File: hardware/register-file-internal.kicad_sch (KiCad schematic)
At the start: 7 parts, among them U4 CD74HC670M96, U5 CD74HC670M96, U6 SN74LVC8T245DWRG4

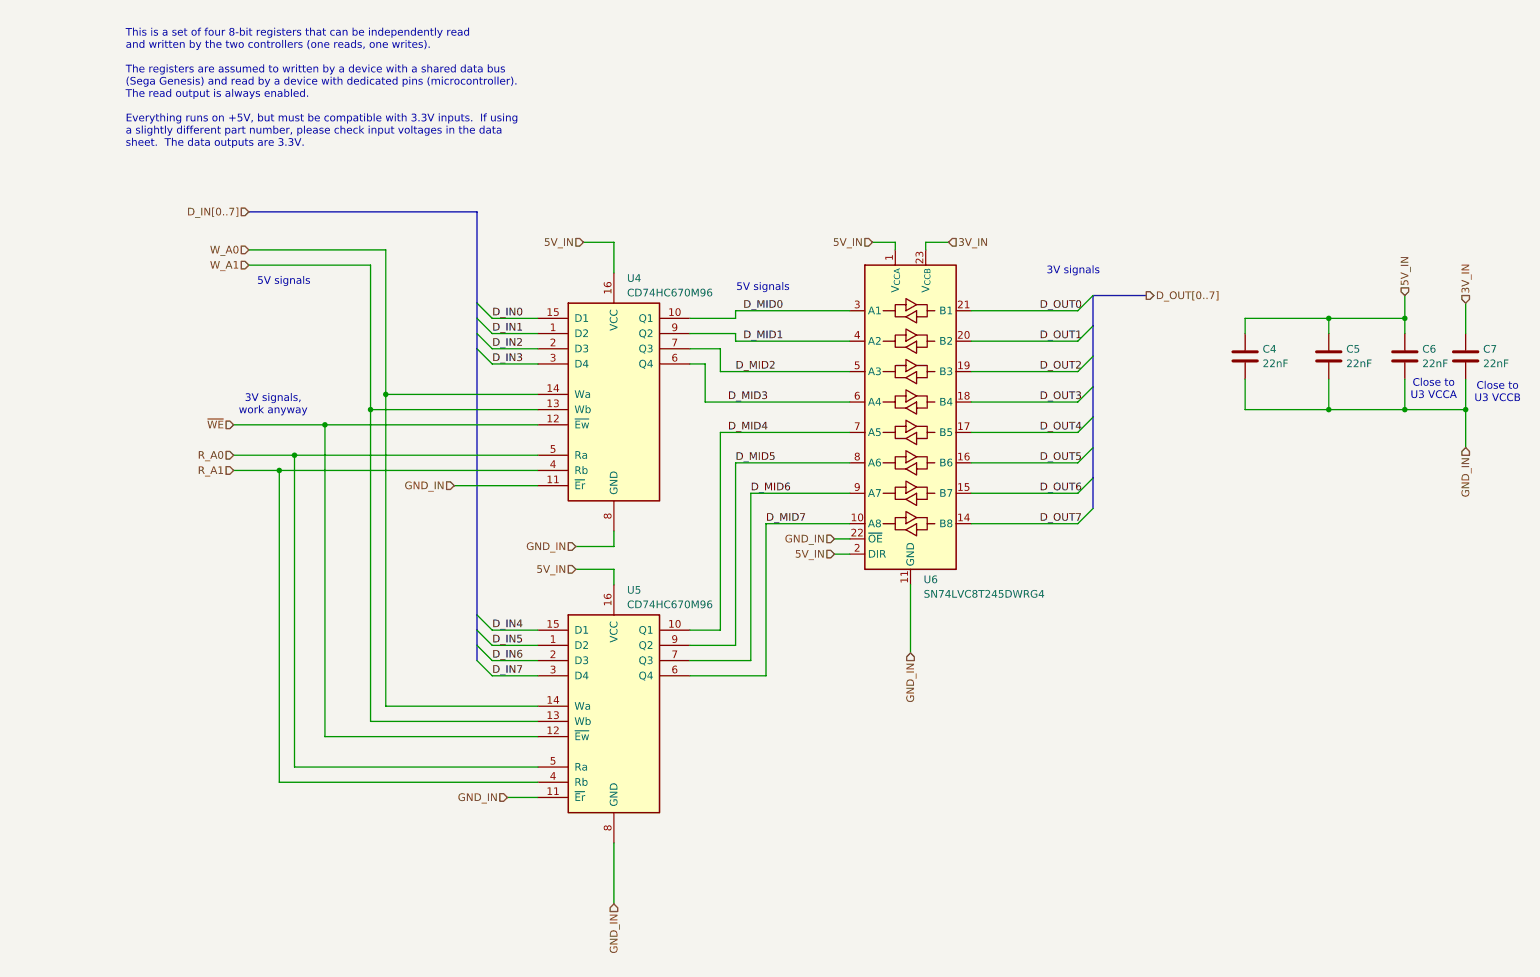
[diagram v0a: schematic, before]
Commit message: Massively reorganize board designs
Now planning to have most assembly done by JLCPCB, so trace sizes,
part selections, etc. are set accordingly.

New boards are:
 - cartridge interface & flash
 - microcontroller & registers
 - sram x2
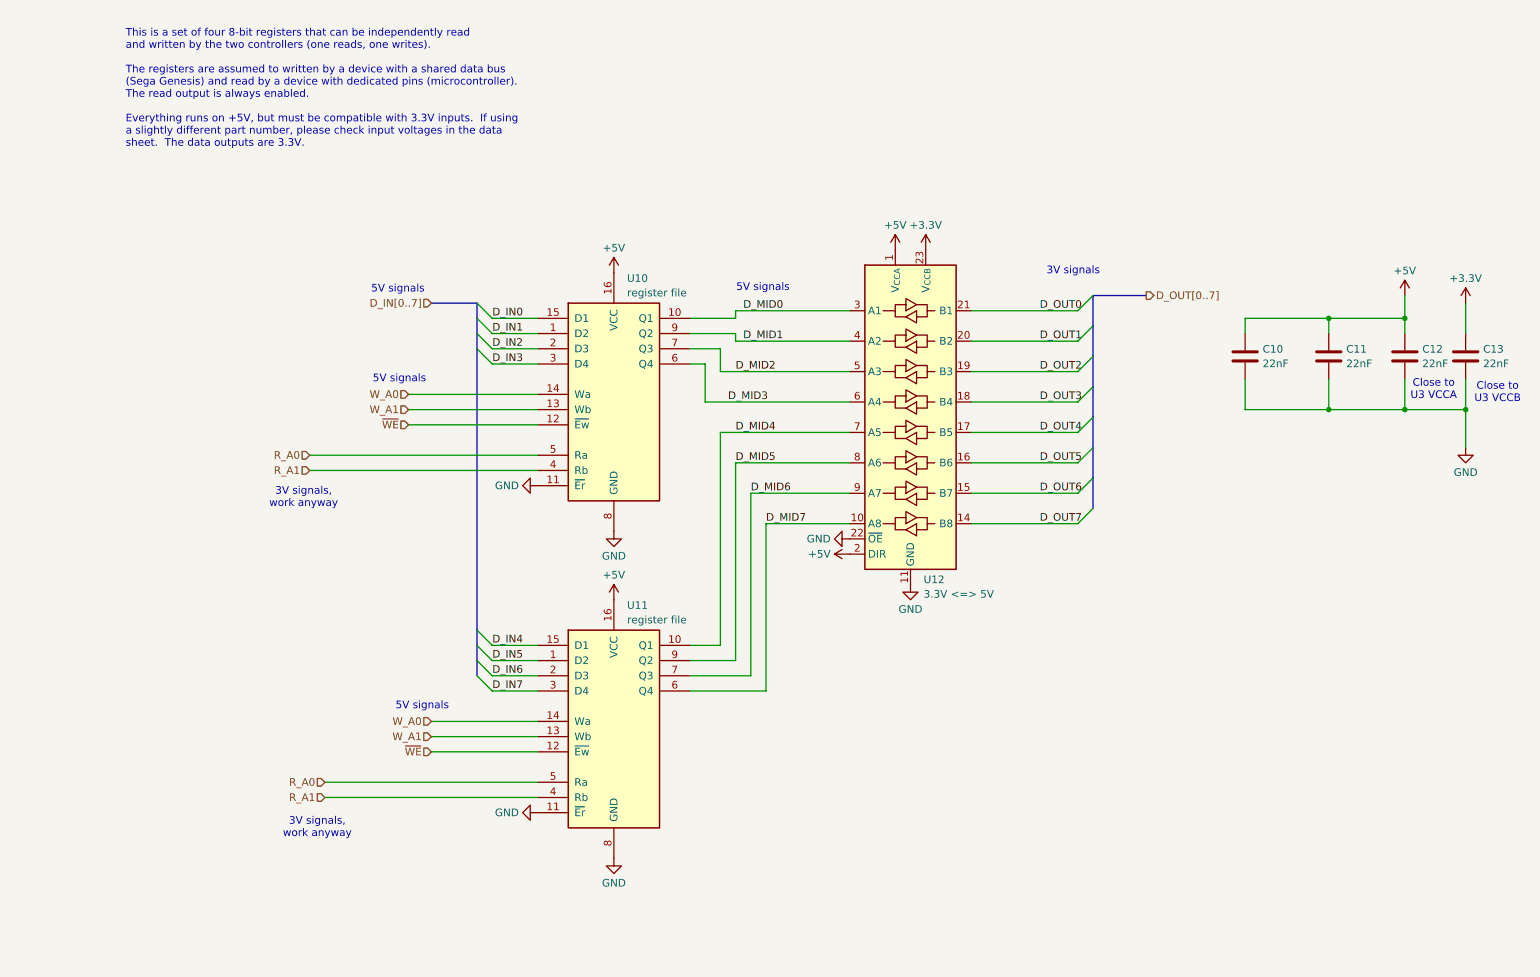
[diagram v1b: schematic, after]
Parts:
- C10: renamed from C4; JLCPCB Part Number (none) -> C21122; Mouser Part Number (none) -> 187-CL10B223KB8NNNC; Part Number (none) -> CL10B223KB8NNNC
- C11: renamed from C5; JLCPCB Part Number (none) -> C21122; Mouser Part Number (none) -> 187-CL10B223KB8NNNC; Part Number (none) -> CL10B223KB8NNNC
- C12: renamed from C6; JLCPCB Part Number (none) -> C21122; Mouser Part Number (none) -> 187-CL10B223KB8NNNC; Part Number (none) -> CL10B223KB8NNNC
- C13: renamed from C7; JLCPCB Part Number (none) -> C21122; Mouser Part Number (none) -> 187-CL10B223KB8NNNC; Part Number (none) -> CL10B223KB8NNNC
- U10: renamed from U4; value CD74HC670M96 -> register file; Mouser Part Number (none) -> 595-CD74HC670M96; Part Number (none) -> CD74HC670M96
- U11: renamed from U5; value CD74HC670M96 -> register file; Mouser Part Number (none) -> 595-CD74HC670M96; Part Number (none) -> CD74HC670M96
- U12: renamed from U6; value SN74LVC8T245DWRG4 -> 3.3V <=> 5V; footprint Package_SO:SOIC-24W_7.5x15.4mm_P1.27mm -> Package_SO:SSOP-24_5.3x8.2mm_P0.65mm; JLCPCB Part Number (none) -> C19197; Mouser Part Number (none) -> 595-SN74LVC8T245DBR; Part Number (none) -> SN74LVC8T245DBR
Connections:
- net 3V_IN renamed +3.3V
- net 5V_IN renamed +5V
- net GND_IN renamed GND
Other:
- moved on the sheet: U11

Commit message: Revise microcontroller board based on latest cart board improvements
 - Update comments
 - Segregate the Ethernet module's power supply so it can be
   disconnected if something goes wrong in a prototype
 - Update board setup to match latest cart board
 - Remove unnecessary level-shifter
 - Fix address decoder to non-latching version
 - Fix address decoder output assignment
 - Consolidate buffer ICs in register file
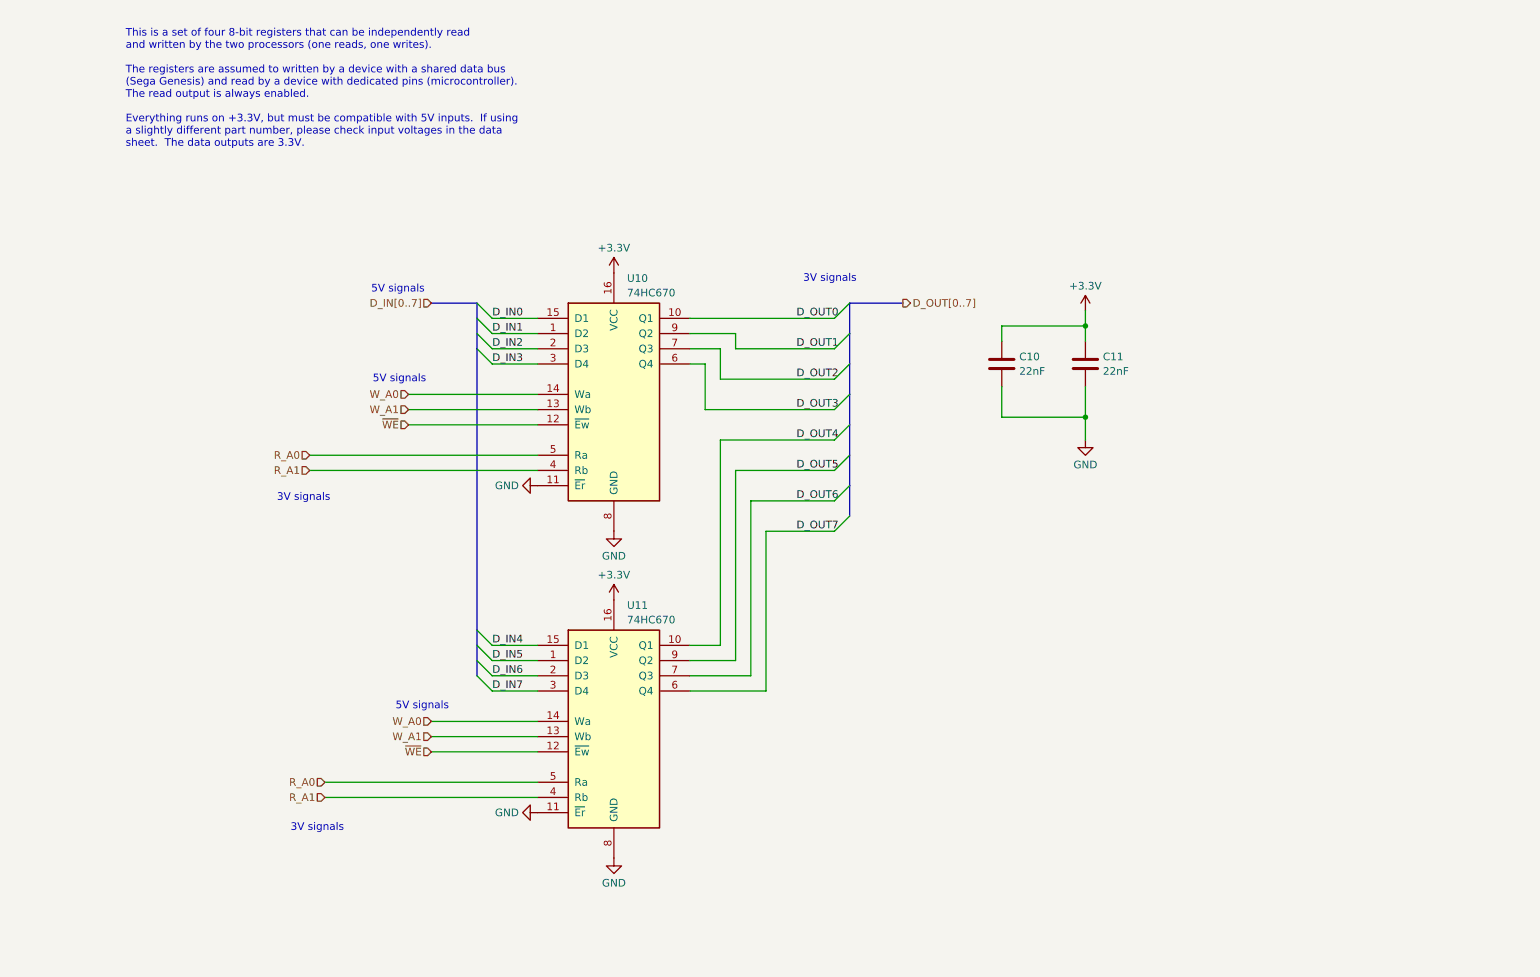
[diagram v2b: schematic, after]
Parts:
- removed C12, C13: 22nF, Capacitor_SMD:C_0603_1608Metric, symbol Device:C
- removed U12: 3.3V <=> 5V, Package_SO:SSOP-24_5.3x8.2mm_P0.65mm, symbol Logic_LevelTranslator:SN74LVC8T245
- U10, U11: value register file -> 74HC670
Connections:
- net +5V is gone; now on net +3.3V: C10.1, C11.1, U10.16 (VCC), U11.16 (VCC)
- net D_MID0 is gone; now on net D_OUT0: U10.10 (Q1)
- net D_MID1 is gone; now on net D_OUT1: U10.9 (Q2)
- net D_MID2 is gone; now on net D_OUT2: U10.7 (Q3)
- net D_MID3 is gone; now on net D_OUT3: U10.6 (Q4)
- net D_MID4 is gone; now on net D_OUT4: U11.10 (Q1)
- net D_MID5 is gone; now on net D_OUT5: U11.9 (Q2)
- net D_MID6 is gone; now on net D_OUT6: U11.7 (Q3)
- net D_MID7 is gone; now on net D_OUT7: U11.6 (Q4)
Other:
- note added: "This is a set of four 8-bit registers that can be independently read and written by the two processors (one reads, one writes). The registers are assumed to written by a device with a shared data bus (Sega Genesis) and read by a device with dedicated pins (microcontroller). The read output is always enabled. Everything runs on +3.3V, but must be compatible with 5V inputs. If using a slightly diff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"
- note removed: "3V signals, work anyway"
- note removed: "Close to U3 VCCA"
- note removed: "Close to U3 VCCB"
- note removed: "This is a set of four 8-bit registers that can be independently read and written by the two controllers (one reads, one writes). The registers are assumed to written by a device with a shared data bus (Sega Genesis) and read by a device with dedicated pins (microcontroller). The read output is always enabled. Everything runs on +5V, but must be compatible with 3.3V inputs. If using a slightly dif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"
- moved on the sheet: C10, C11

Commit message: Revise microcontroller board based on latest cart board improvements
 - Update comments
 - Segregate the Ethernet module's power supply so it can be
   disconnected if something goes wrong in a prototype
 - Update board setup to match latest cart board
 - Remove unnecessary level-shifter
 - Fix address decoder to non-latching version
 - Fix address decoder output assignment
 - Consolidate buffer ICs in register file
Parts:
- U10, U11: JLCPCB Part Number (none) -> C206182
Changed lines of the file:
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@@
 			)
 		)
-		(property "JLCPCB Part Number" ""
+		(property "JLCPCB Part Number" "C206182"
 			(at 109.22 149.86 0)
 			(effects
@@
 			)
 		)
-		(property "JLCPCB Part Number" ""
+		(property "JLCPCB Part Number" "C206182"
 			(at 109.22 95.25 0)
 			(effects

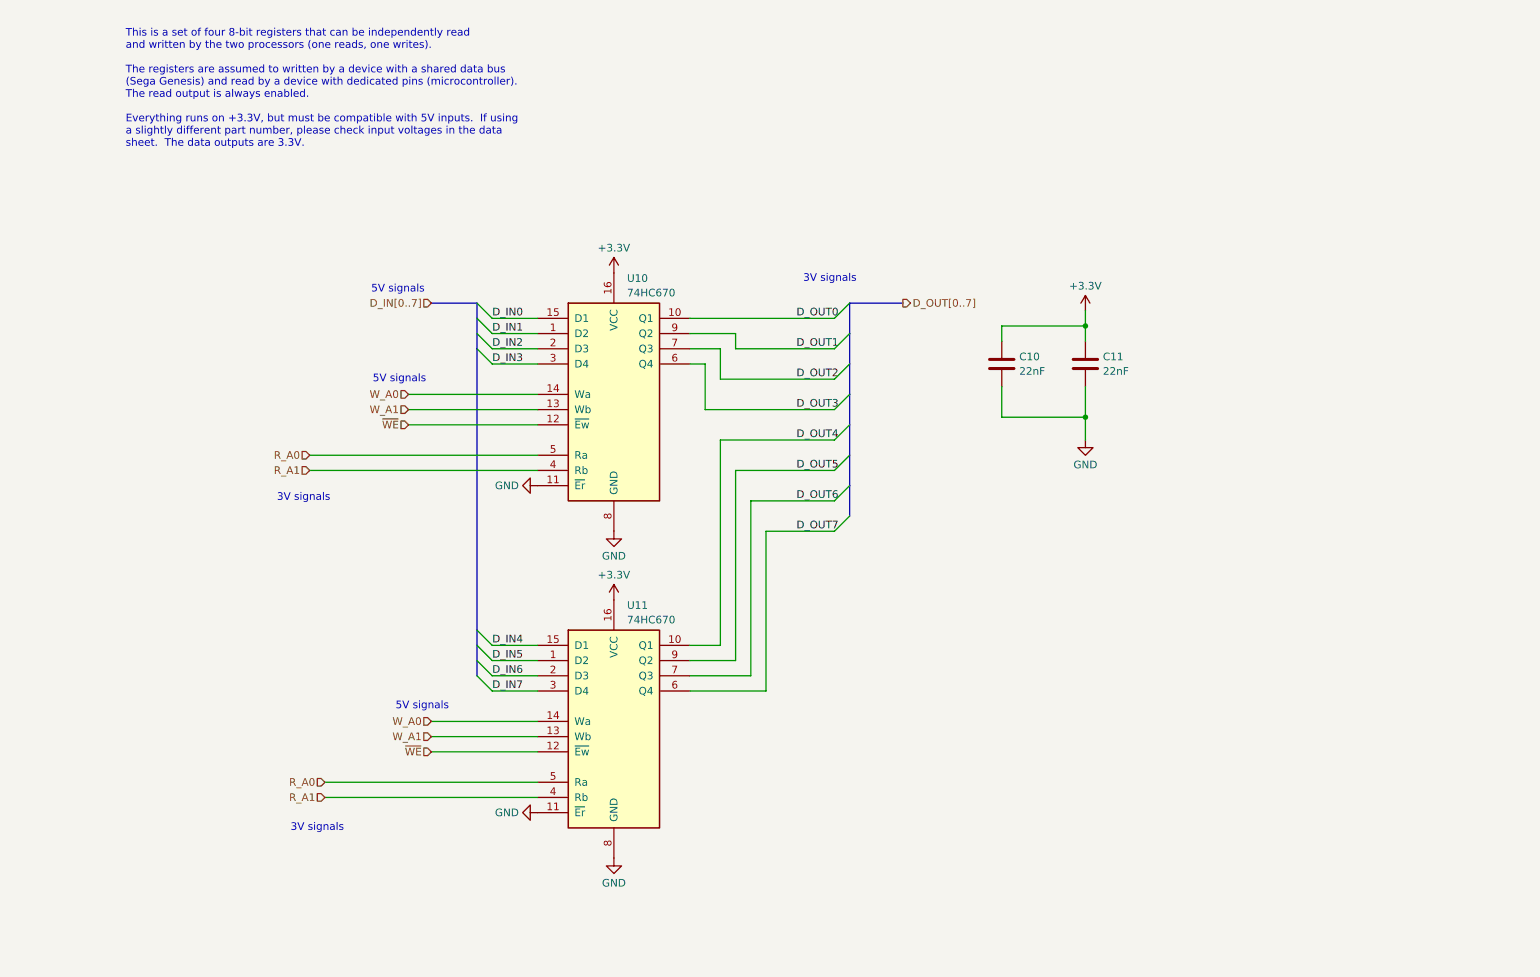
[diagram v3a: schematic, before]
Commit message: Improve uC board assembly further
Change the register file CD74HC670M96 with SN74AHC373PWR and an
inverter, which is more easily available from JLCPCB.

This is not an exact replacement, as we replaced 2x 4x4 register files
with 2x 8-bit latches.  So instead of 4x 8-bit registers, we now only
have 2x 8-bit registers, but we only used 2 to begin with.

The new register hardware required us to change the address decoding
and the actual addresses of the registers.  Instead of 0xA13000 and
0xA13002, we now write to 0xA13010 and 0xA13012.
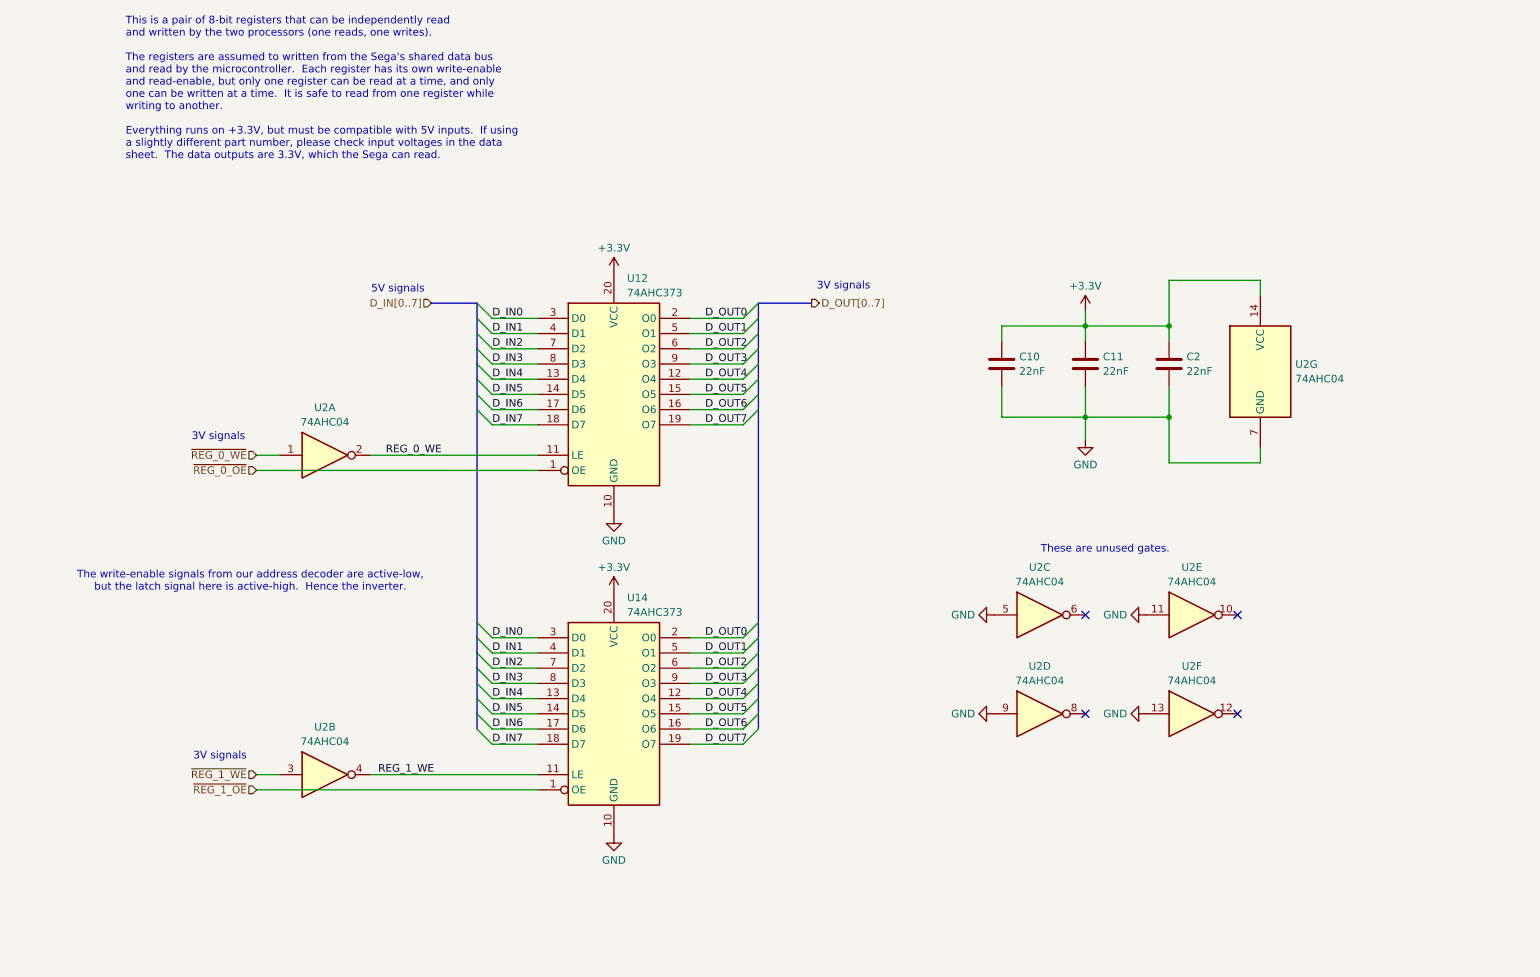
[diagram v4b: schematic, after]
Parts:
- removed U10, U11: 74HC670, Package_SO:SOIC-16_3.9x9.9mm_P1.27mm, symbol 74xx:74LS670
- added C2: 22nF, Capacitor_SMD:C_0603_1608Metric, symbol Device:C
- added U12, U14: 74AHC373, Package_SO:TSSOP-20_4.4x6.5mm_P0.65mm, symbol 74xx:74LS373
- added U2: 74AHC04, Package_SO:TSSOP-14_4.4x5mm_P0.65mm, symbol 74xx:74AHC04
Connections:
- net +3.3V: now also C2.1, U12.20 (VCC), U14.20 (VCC), U2.14 (VCC)
- net D_IN0: now also U12.3 (D0), U14.3 (D0)
- net D_IN1: now also U12.4 (D1), U14.4 (D1)
- net D_IN2: now also U12.7 (D2), U14.7 (D2)
- net D_IN3: now also U12.8 (D3), U14.8 (D3)
- net D_IN4: now also U12.13 (D4), U14.13 (D4)
- net D_IN5: now also U12.14 (D5), U14.14 (D5)
- net D_IN6: now also U12.17 (D6), U14.17 (D6)
- net D_IN7: now also U12.18 (D7), U14.18 (D7)
- net D_OUT0: now also U12.2 (O0), U14.2 (O0)
- net D_OUT1: now also U12.5 (O1), U14.5 (O1)
- net D_OUT2: now also U12.6 (O2), U14.6 (O2)
- net D_OUT3: now also U12.9 (O3), U14.9 (O3)
- net D_OUT4: now also U12.12 (O4), U14.12 (O4)
- net D_OUT5: now also U12.15 (O5), U14.15 (O5)
- net D_OUT6: now also U12.16 (O6), U14.16 (O6)
- net D_OUT7: now also U12.19 (O7), U14.19 (O7)
- net GND: now also C2.2, U12.10 (GND), U14.10 (GND), U2.11, U2.13, U2.5, U2.7 (GND), U2.9
- new net REG_0_WE: U12.11 (LE), U2.2
- new net REG_1_WE: U14.11 (LE), U2.4
- new net ~{REG_0_OE}: U12.1 (OE)
- new net ~{REG_0_WE}: U2.1
- new net ~{REG_1_OE}: U14.1 (OE)
- new net ~{REG_1_WE}: U2.3
- no-connect marks 0 -> 4
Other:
- note added: "The write-enable signals from our address decoder are active-low, but the latch signal here is active-high. Hence the inverter."
- note added: "These are unused gates."
- note added: "This is a pair of 8-bit registers that can be independently read and written by the two processors (one reads, one writes). The registers are assumed to written from the Sega's shared data bus and read by the microcontroller. Each register has its own write-enable and read-enable, but only one register can be read at a time, and only one can be written at a time. It is safe to read from one regis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"
- note removed: "This is a set of four 8-bit registers that can be independently read and written by the two processors (one reads, one writes). The registers are assumed to written by a device with a shared data bus (Sega Genesis) and read by a device with dedicated pins (microcontroller). The read output is always enabled. Everything runs on +3.3V, but must be compatible with 5V inputs. If using a slightly diff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"
